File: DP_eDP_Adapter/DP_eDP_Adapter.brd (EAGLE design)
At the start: 50 x 50 mm, 15 parts, among them IC1 TLC5947XLP, IC2 REG1117M3.3

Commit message: 
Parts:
- C1, C2: device SparkFun:0603-CAP -> SparkFun:0402-CAP
- R2: device SparkFun-Passives:0603-RES -> SparkFun-Passives:0402-RES
- moved SIG_OUT 8.28 mm to (8.23, 9.65)
- moved SIG_IN 5.59 mm to (15.5, 9.65)
- moved C2 1.06 mm to (7.98, -0.10)
- moved R2 0.56 mm to (6.77, -0.12)
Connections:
- net N$11 renamed LED_NEG_1A
- net N$15 renamed LED_NEG_2A
- net N$16 renamed LED_NEG_3A
- net N$17 renamed LED_NEG_4A
- net N$18 renamed LED_NEG_5A
- net N$19 renamed LED_NEG_6A
- net N$20 renamed LED_NEG_1B
- net N$21 renamed LED_NEG_2B
- net N$22 renamed LED_NEG_3B
- net N$23 renamed LED_NEG_4B
- net N$24 renamed LED_NEG_5B
- net N$25 renamed LED_NEG_6B
- removed net N$26: SV1.P$45
- removed net N$27: SV1.P$46
- removed net N$28: SV1.P$48
- removed net N$29: SV1.P$49
- new net LED_POS_1: SV1.P$48, SV1.P$49
- new net LED_POS_2: SV1.P$45, SV1.P$46
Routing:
- net BLANK: track 0.00 -> 29.0 mm, vias 0 -> 1
- net XLAT: track 6.24 -> 32.8 mm, vias 0 -> 1
- net SCLK: track 0.00 -> 25.3 mm, vias 0 -> 1
- net SIN: track 0.00 -> 17.0 mm
- net LED_POS_1: track 0.00 -> 2.08 mm
- net LED_POS_2: track 0.00 -> 2.07 mm
- net +3V3: track 30.3 -> 31.8 mm
- net GND: track 3.34 -> 2.81 mm
- net SOUT: vias 2 -> 1

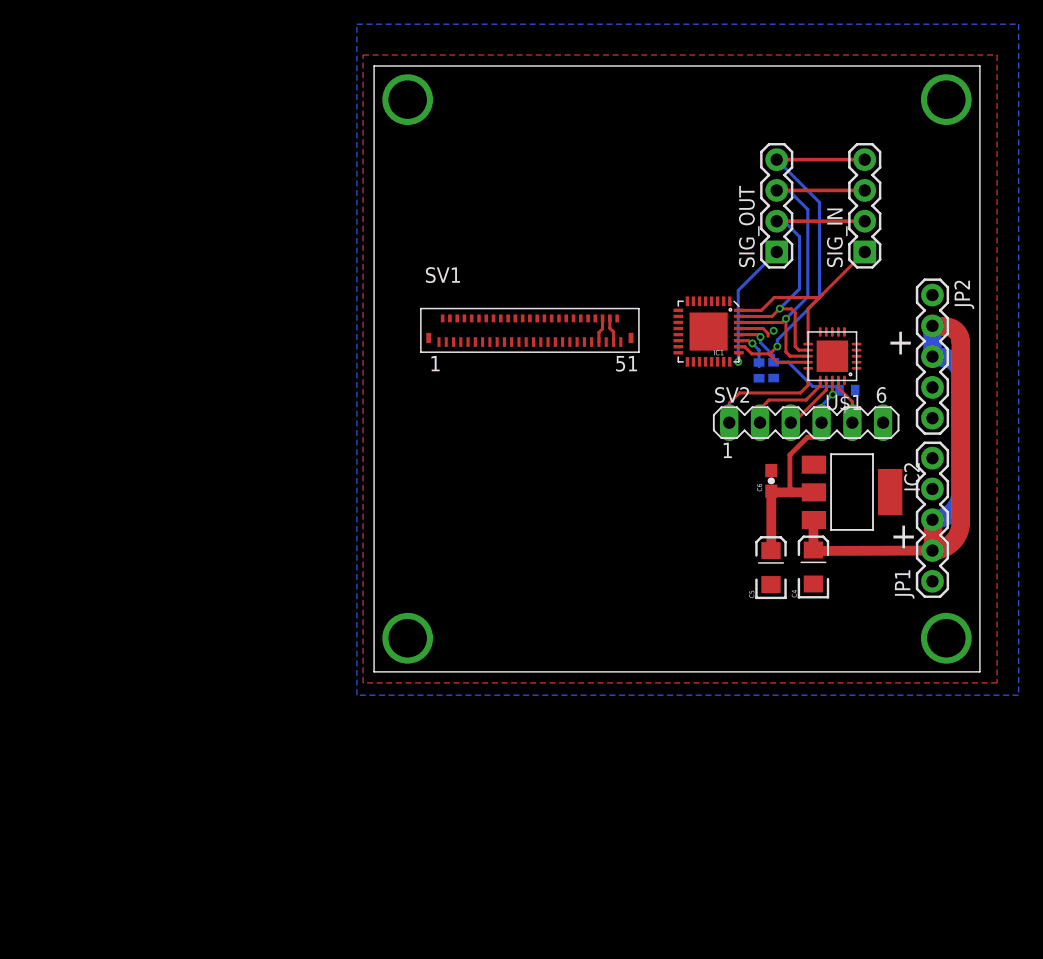
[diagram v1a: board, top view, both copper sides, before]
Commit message: 
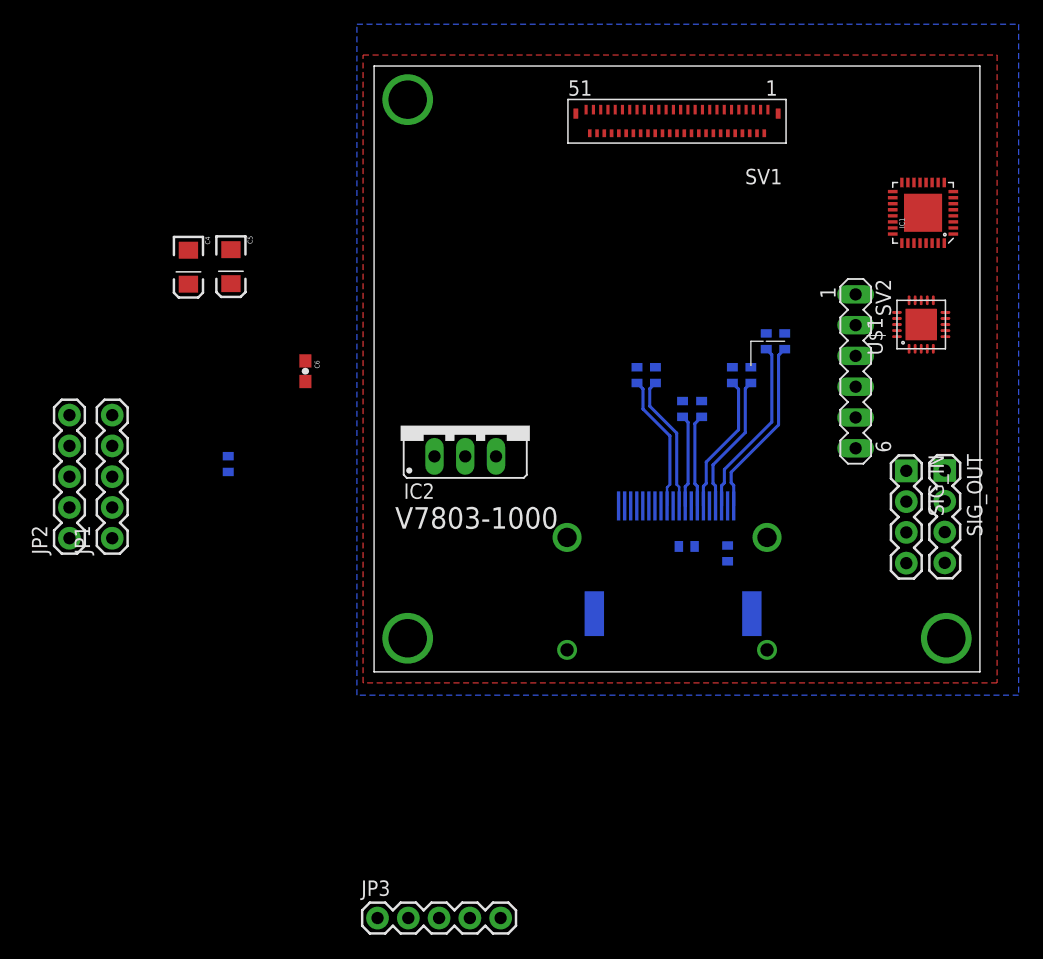
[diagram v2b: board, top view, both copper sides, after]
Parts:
- added C10, C11, C12, C13, C3, C7, C8, C9: (no value), DP_eDP_Adapter:SPARKFUN-PASSIVES_0402-CAP
- added JP3: (no value), SparkFun-Connectors:1X05
- added U$2: DP1RD20JQ2R400, DP_eDP_Adapter:DP_REVERSE_JAE
- IC2: value REG1117M3.3 -> (none); device burr-brown:SOT223 -> v-reg:78XXS
- JP1: value Power IN -> (none)
- moved JP2 74.0 mm to (-50.1, -14.0), turned to 90 degrees
- moved JP1 67.8 mm to (-46.6, -14.0)
- moved C4 57.2 mm to (-40.3, 8.39), turned to 270 degrees
- moved C5 51.0 mm to (-36.8, 8.44), turned to 270 degrees
- moved C2 45.7 mm to (-37.0, -7.85), turned to 90 degrees
- moved C6 39.5 mm to (-30.7, -0.19), turned to 270 degrees
- moved IC2 32.4 mm to (-17.5, -4.67), turned to 0 degrees
- moved SIG_OUT 22.7 mm to (22.1, -8.38), turned to 270 degrees
- moved SV1 20.9 mm to (0.00, 20.3), turned to 180 degrees
- moved IC1 20.2 mm to (20.3, 12.9), turned to 90 degrees
- moved C1 18.5 mm to (0.80, -14.6), turned to 0 degrees
- moved SIG_IN 18.4 mm to (18.9, -8.41), turned to 270 degrees
- moved R2 15.3 mm to (4.18, -15.2), turned to 270 degrees
- moved U$1 7.78 mm to (20.2, 3.67), turned to 90 degrees
- moved SV2 5.88 mm to (14.7, -0.20), turned to 270 degrees
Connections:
- new net N$15_N: C9.1, U$2.P$6
- new net N$15_P: C8.1, U$2.P$4
- new net N$17_N: C11.1, U$2.P$9
- new net N$17_P: C10.1, U$2.P$7
- new net N$19_N: C13.1, U$2.P$12
- new net N$19_P: C12.1, U$2.P$10
- new net N$3_N: C7.1, U$2.P$3
- new net N$3_P: C3.1, U$2.P$1
- net +3V3: no longer IC2.2
- net 20V: now also JP3.2, JP3.3; no longer IC2.3
- net GND: now also JP3.4, JP3.5, U$2.P$11, U$2.P$16, U$2.P$2, U$2.P$5, U$2.P$8; no longer IC2.1
- net LANE0_N: now also C7.2
- net LANE0_P: now also C3.2
- net LANE1_N: now also C9.2
- net LANE1_P: now also C8.2
- net LANE2_N: now also C11.2
- net LANE2_P: now also C10.2
- net LANE3_N: now also C13.2
- net LANE3_P: now also C12.2
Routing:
- net 20V: track 54.4 -> 0.00 mm
- net XLAT: track 32.8 -> 0.00 mm, vias 1 -> 0
- net +3V3: track 31.8 -> 0.00 mm, vias 2 -> 0
- net BLANK: track 29.0 -> 0.00 mm, vias 1 -> 0
- net SCLK: track 25.3 -> 0.00 mm, vias 1 -> 0
- net SIN: track 17.0 -> 0.00 mm
- net N$3_P: track 0.00 -> 14.9 mm
- net N$3_N: track 0.00 -> 14.8 mm
- net N$15_N: track 0.00 -> 11.6 mm
- net N$15_P: track 0.00 -> 11.5 mm
- net N$19_N: track 0.00 -> 11.4 mm
- net N$19_P: track 0.00 -> 11.3 mm
- net SOUT: track 11.2 -> 0.00 mm, vias 1 -> 0
- net MOSI: track 10.1 -> 0.00 mm
- net N$17_P: track 0.00 -> 7.67 mm
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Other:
- board text added: "V7803-1000"
- board text removed: "+"

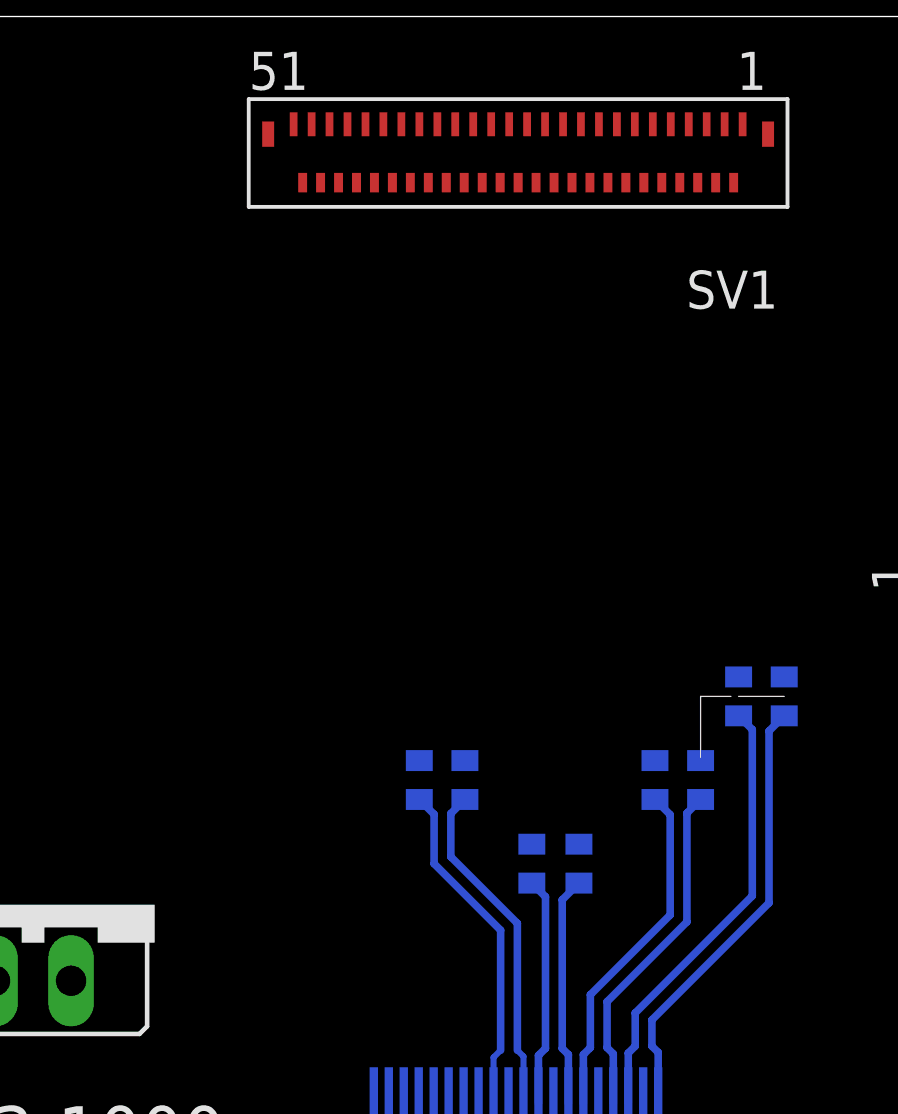
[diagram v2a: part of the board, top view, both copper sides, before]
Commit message: 
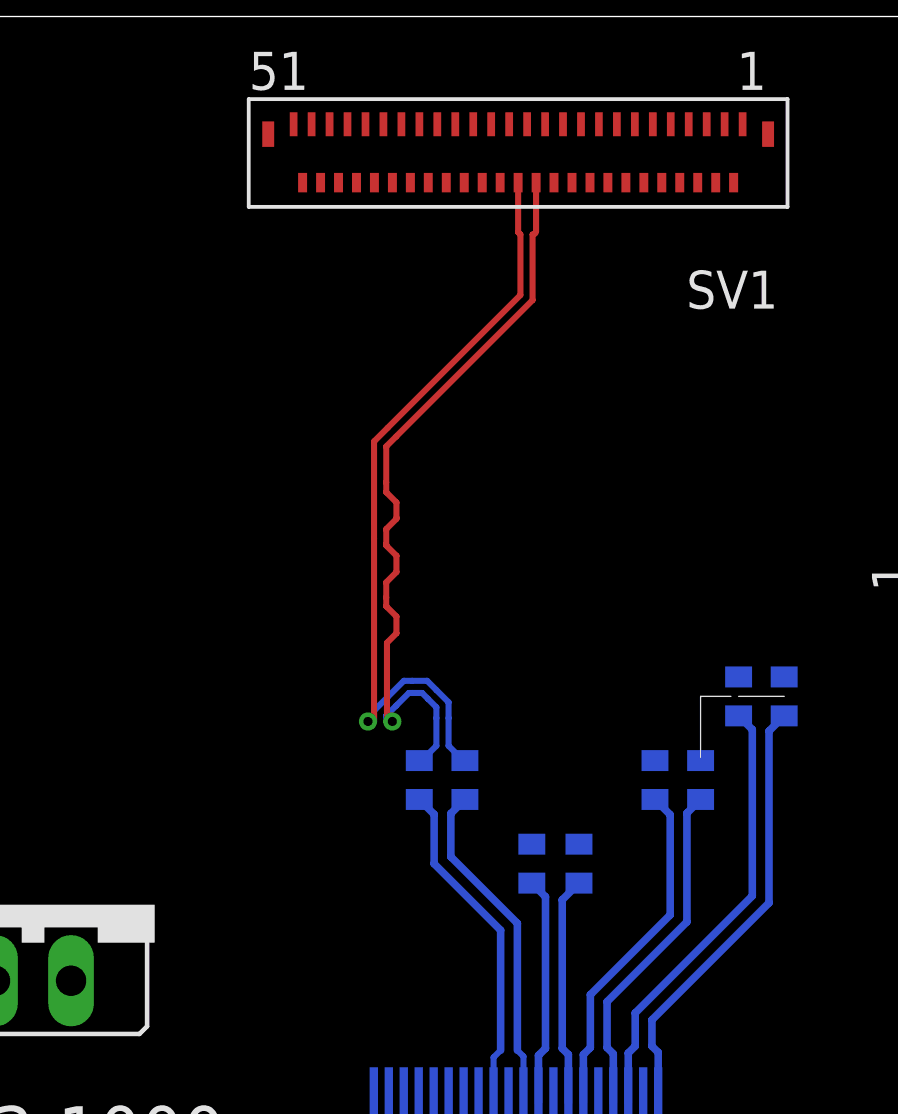
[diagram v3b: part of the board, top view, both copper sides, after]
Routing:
- net LANE3_P: track 0.00 -> 26.2 mm, vias 0 -> 1
- net LANE3_N: track 0.00 -> 25.7 mm, vias 0 -> 1
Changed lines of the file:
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@@
 <contactref element="SV1" pad="P$24"/>
 <contactref element="C13" pad="2"/>
-<wire x1="-3.302" y1="0.142" x2="0.6" y2="19.45" width="0" layer="19" extent="1-16"/>
+<wire x1="-3.302" y1="0.142" x2="-3.2235" y2="0.142" width="0.2032" layer="16"/>
+<wire x1="-3.2235" y1="0.142" x2="-2.7305" y2="0.635" width="0.2032" layer="16"/>
+<wire x1="-2.7305" y1="1.5621" x2="-2.7305" y2="0.635" width="0.2032" layer="16"/>
+<wire x1="-2.7305" y1="1.5621" x2="-2.7305" y2="1.92243125" width="0.2032" layer="16"/>
+<wire x1="-2.7305" y1="1.92243125" x2="-3.013884375" y2="2.205815625" width="0.2032" layer="16"/>
+<wire x1="-3.013884375" y1="2.205815625" x2="-3.20836875" y2="2.4003" width="0.2032" layer="16"/>
+<wire x1="-3.20836875" y1="2.4003" x2="-3.5433" y2="2.4003" width="0.2032" layer="16"/>
+<wire x1="-3.5433" y1="2.4003" x2="-3.64963125" y2="2.4003" width="0.2032" layer="16"/>
+<wire x1="-3.64963125" y1="2.4003" x2="-4.072715625" y2="1.977215625" width="0.2032" layer="16"/>
+<wire x1="-4.072715625" y1="1.977215625" x2="-4.4069" y2="1.64303125" width="0.2032" layer="16"/>
+<wire x1="-4.4069" y1="1.64303125" x2="-4.4069" y2="1.4478" width="0.2032" layer="16"/>
+<via x="-4.2037" y="1.4478" extent="1-16" drill="0.3048"/>
+<wire x1="-4.4069" y1="1.4478" x2="-4.2037" y2="1.4478" width="0.2032" layer="16"/>
+<wire x1="-4.3815" y1="4.0767" x2="-4.3815" y2="1.4478" width="0.2032" layer="1"/>
+<wire x1="-4.4069" y1="10.63463125" x2="-4.072715625" y2="10.968815625" width="0.2032" layer="1"/>
+<wire x1="0.4826" y1="15.52413125" x2="-4.072715625" y2="10.968815625" width="0.2032" layer="1"/>
+<wire x1="0.4826" y1="15.52413125" x2="0.4826" y2="17.7165" width="0.2032" layer="1"/>
+<wire x1="0.6" y1="19.45" x2="0.6" y2="17.8339" width="0.2032" layer="1"/>
+<wire x1="0.6" y1="17.8339" x2="0.4826" y2="17.7165" width="0.2032" layer="1" curve="-90"/>
+<wire x1="-4.4069" y1="9.4361" x2="-4.4069" y2="10.63463125" width="0.2032" layer="1"/>
+<wire x1="-4.3815" y1="1.4478" x2="-4.2037" y2="1.4478" width="0.2032" layer="1"/>
+<wire x1="-4.4069" y1="9.4361" x2="-4.4069" y2="9.1059" width="0.2032" layer="1"/>
+<wire x1="-4.4069" y1="9.1059" x2="-4.064" y2="8.763" width="0.2032" layer="1"/>
+<wire x1="-4.064" y1="8.763" x2="-4.064" y2="8.255" width="0.2032" layer="1"/>
+<wire x1="-4.064" y1="8.255" x2="-4.064" y2="8.2169" width="0.2032" layer="1"/>
+<wire x1="-4.064" y1="8.2169" x2="-4.4069" y2="7.874" width="0.2032" layer="1"/>
+<wire x1="-4.4069" y1="7.874" x2="-4.4069" y2="7.366" width="0.2032" layer="1"/>
+<wire x1="-4.4069" y1="7.366" x2="-4.4069" y2="7.3279" width="0.2032" layer="1"/>
+<wire x1="-4.4069" y1="7.3279" x2="-4.064" y2="6.985" width="0.2032" layer="1"/>
+<wire x1="-4.064" y1="6.985" x2="-4.064" y2="6.4389" width="0.2032" layer="1"/>
+<wire x1="-4.064" y1="6.4389" x2="-4.4069" y2="6.096" width="0.2032" layer="1"/>
+<wire x1="-4.4069" y1="6.096" x2="-4.4069" y2="5.588" width="0.2032" layer="1"/>
+<wire x1="-4.4069" y1="5.588" x2="-4.4069" y2="5.2959" width="0.2032" layer="1"/>
+<wire x1="-4.4069" y1="5.2959" x2="-4.064" y2="4.953" width="0.2032" layer="1"/>
+<wire x1="-4.064" y1="4.953" x2="-4.064" y2="4.3942" width="0.2032" layer="1"/>
+<wire x1="-4.064" y1="4.3942" x2="-4.3815" y2="4.0767" width="0.2032" layer="1"/>
 </signal>
 <signal name="LANE3_P" class="1">
 <contactref element="SV1" pad="P$26"/>
 <contactref element="C12" pad="2"/>
-<wire x1="-1.778" y1="0.142" x2="0" y2="19.45" width="0" layer="19" extent="1-16"/>
+<wire x1="-1.778" y1="0.142" x2="-1.8311" y2="0.142" width="0.2032" layer="16"/>
+<wire x1="-1.8311" y1="0.142" x2="-2.3241" y2="0.635" width="0.2032" layer="16"/>
+<wire x1="-2.3241" y1="1.5621" x2="-2.3241" y2="0.635" width="0.2032" layer="16"/>
+<wire x1="-2.3241" y1="1.5621" x2="-2.3241" y2="2.09076875" width="0.2032" layer="16"/>
+<wire x1="-2.3241" y1="2.09076875" x2="-2.726515625" y2="2.493184375" width="0.2032" layer="16"/>
+<wire x1="-2.726515625" y1="2.493184375" x2="-3.04003125" y2="2.8067" width="0.2032" layer="16"/>
+<wire x1="-3.04003125" y1="2.8067" x2="-3.5433" y2="2.8067" width="0.2032" layer="16"/>
+<wire x1="-3.5433" y1="2.8067" x2="-3.81796875" y2="2.8067" width="0.2032" layer="16"/>
+<wire x1="-3.81796875" y1="2.8067" x2="-4.360084375" y2="2.264584375" width="0.2032" layer="16"/>
+<wire x1="-4.360084375" y1="2.264584375" x2="-4.8133" y2="1.81136875" width="0.2032" layer="16"/>
+<wire x1="-4.8133" y1="1.81136875" x2="-4.8133" y2="1.4478" width="0.2032" layer="16"/>
+<via x="-5.0165" y="1.4478" extent="1-16" drill="0.3048"/>
+<wire x1="-4.8133" y1="1.4478" x2="-5.0165" y2="1.4478" width="0.2032" layer="1"/>
+<wire x1="-4.8133" y1="1.4478" x2="-5.0165" y2="1.4478" width="0.2032" layer="16"/>
+<wire x1="-4.8133" y1="7.56446875" x2="-4.8133" y2="1.4478" width="0.2032" layer="1"/>
+<wire x1="-4.8133" y1="8.11056875" x2="-4.8133" y2="7.56446875" width="0.2032" layer="1"/>
+<wire x1="-4.8133" y1="8.11056875" x2="-4.8133" y2="10.80296875" width="0.2032" layer="1"/>
+<wire x1="-4.8133" y1="10.80296875" x2="-4.360084375" y2="11.256184375" width="0.2032" layer="1"/>
+<wire x1="0.0762" y1="15.69246875" x2="-4.360084375" y2="11.256184375" width="0.2032" layer="1"/>
+<wire x1="0.0762" y1="15.69246875" x2="0.0762" y2="17.7165" width="0.2032" layer="1"/>
+<wire x1="0.0762" y1="17.7165" x2="0" y2="17.7927" width="0.2032" layer="1"/>
+<wire x1="0" y1="17.7927" x2="0" y2="19.45" width="0.2032" layer="1"/>
 </signal>
 <signal name="N$2">
@@
 <wire x1="0.179" y1="-9.7421" x2="-0.0254" y2="-9.5377" width="0.2032" layer="16"/>
 <wire x1="-0.0254" y1="-5.2944625" x2="-0.0254" y2="-9.5377" width="0.254" layer="16"/>
-<wire x1="-2.2479" y1="-3.0719625" x2="-0.0254" y2="-5.2944625" width="0.254" layer="16"/>
+<wire x1="-0.0254" y1="-5.2944625" x2="-2.2479" y2="-3.0719625" width="0.254" layer="16"/>
 <wire x1="-2.2479" y1="-1.6279" x2="-2.2479" y2="-3.0719625" width="0.254" layer="16"/>
 <wire x1="-1.778" y1="-1.158" x2="-2.2479" y2="-1.6279" width="0.254" layer="16"/>
@@
 <wire x1="-0.821" y1="-9.7745" x2="-0.5842" y2="-9.5377" width="0.2032" layer="16"/>
 <wire x1="-0.5842" y1="-5.5259375" x2="-0.5842" y2="-9.5377" width="0.254" layer="16"/>
-<wire x1="-2.8067" y1="-3.3034375" x2="-0.5842" y2="-5.5259375" width="0.254" layer="16"/>
+<wire x1="-0.5842" y1="-5.5259375" x2="-2.8067" y2="-3.3034375" width="0.254" layer="16"/>
 <wire x1="-2.8067" y1="-1.6533" x2="-2.8067" y2="-3.3034375" width="0.254" layer="16"/>
 <wire x1="-2.8067" y1="-1.6533" x2="-3.302" y2="-1.158" width="0.254" layer="16"/>
